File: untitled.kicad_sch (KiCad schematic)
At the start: 30 parts, among them IC1 ILD206T, IC10 ILD206T, IC2 ILD206T, IC3 ILD206T, IC4 ILD206T, IC5 ILD206T, IC6 ILD206T, IC7 ILD206T, IC8 ILD206T, IC9 ILD206T, J1 1147330000, J2 1147330000, J3 1147330000, K1 G2RL-1-H, K2 G2RL-1-H, K3 G2RL-1-H, U1 ULN2003A, U2 5-1415390-1, U3 5-1415390-1, U4 5-1415390-1

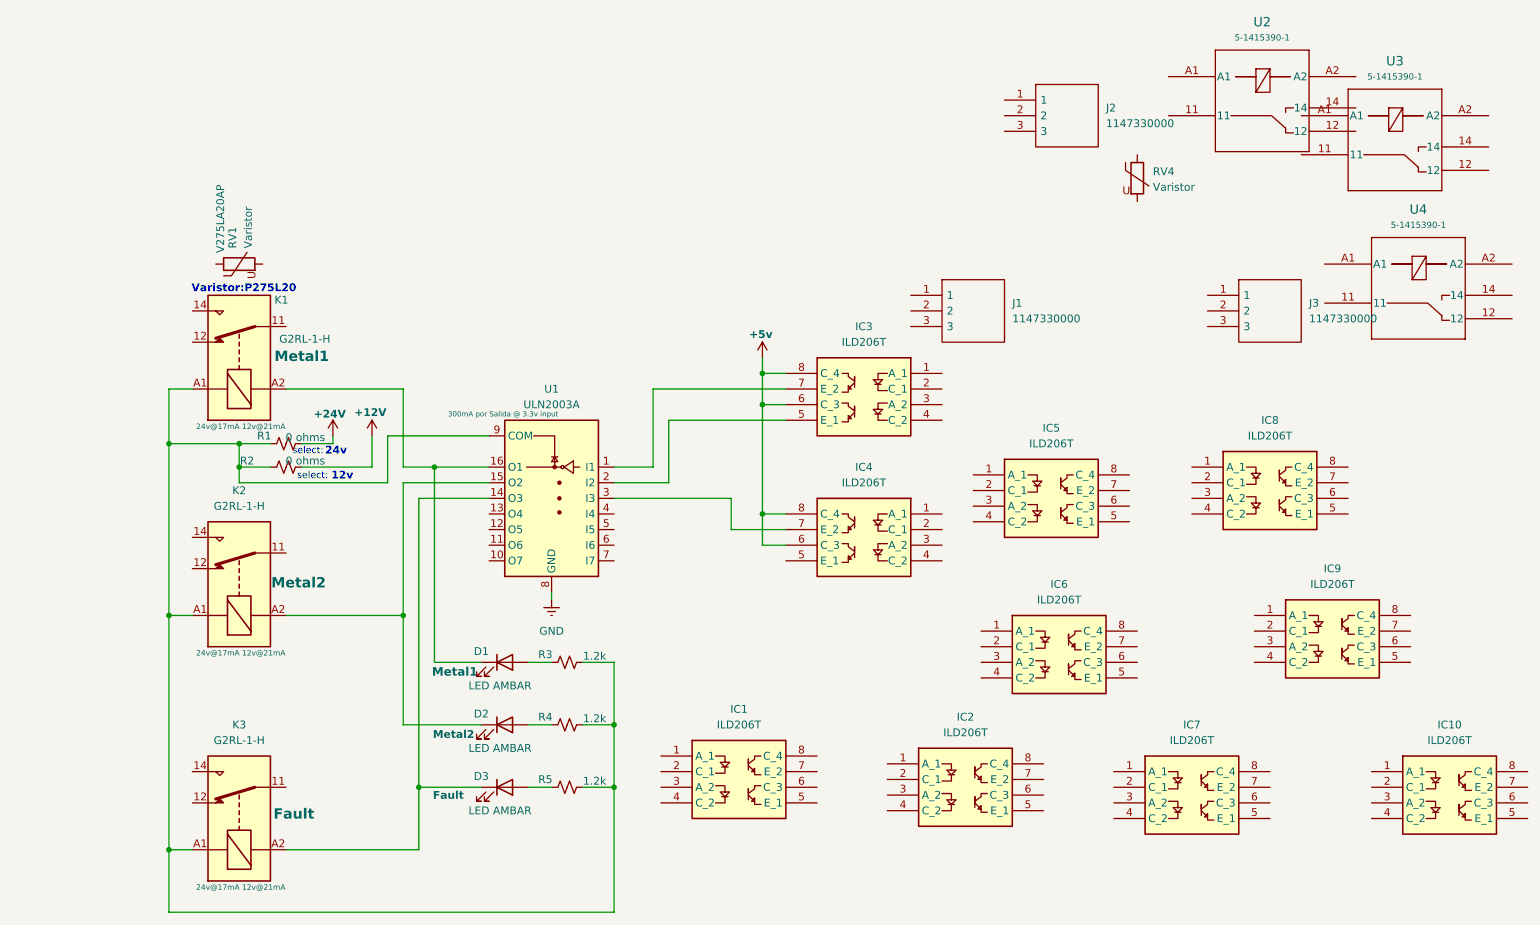
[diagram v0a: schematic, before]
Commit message: 13-Mayo26 se agrego hoja de procesador y USB
hoja de USB AL 95% HOJA DEL procesador al 75%
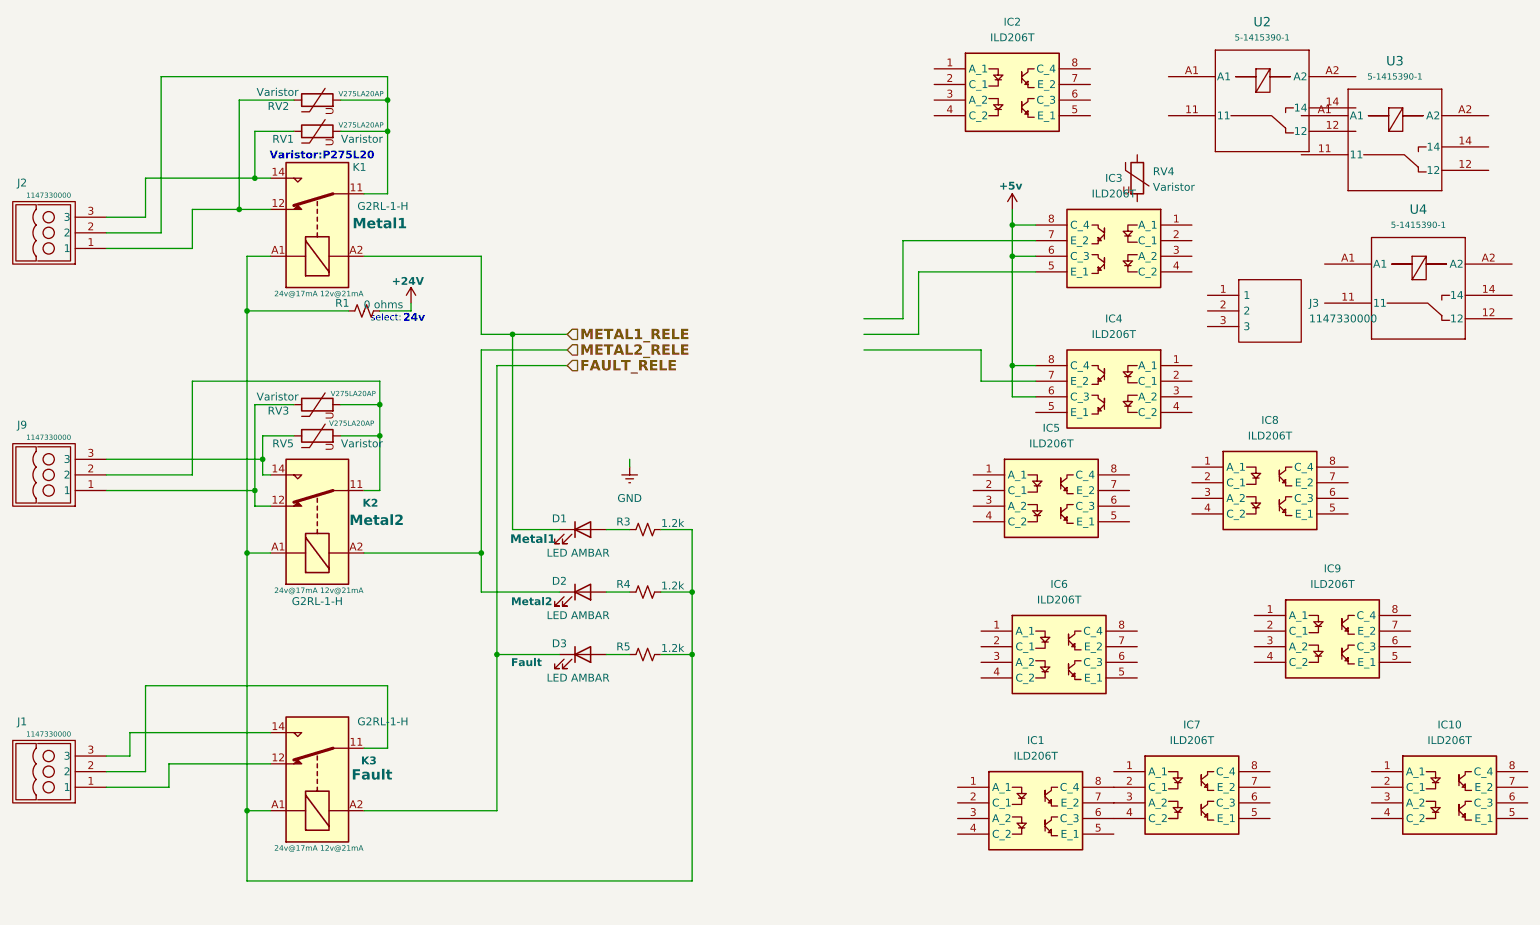
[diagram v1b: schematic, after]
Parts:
- removed R2: 0 ohms, symbol Device:R_Small_US
- removed U1: ULN2003A, symbol Transistor_Array:ULN2003A
- added J9: 1147330000, CONECTORES GRACIDA:3POS-5.08PITCH, symbol CONECTORES GRACIDA:1147330000
- added RV2, RV3, RV5: Varistor, Varistor:RV_Disc_D12mm_W3.9mm_P7.5mm, symbol Device:Varistor
- J1, J2: Mouser (none) -> 470-1147330000; Mouser Part Number 470-1147330000 -> (none); Mouser Price/Stock https://www.mouser.co.uk/ProductDetail/Weidmuller/114733000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 -> (none); Price (none) -> 2.41
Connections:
- net at J1.1: now also K3.12
- net at J1.2: now also K3.11
- net at J1.3: now also K3.14
- net METAL1_RELE: now reaches D1.1 (K), K1.A2
- net at IC1.6 (C_3): now also IC7.4 (C_2)
- net at IC1.7 (E_2): now also IC7.3 (A_2)
- net at IC1.8 (C_4): now also IC7.2 (C_1)
- net FAULT_RELE: now reaches D3.1 (K), K3.A2
- net at K1.11: now also J2.2, RV1.2, RV2.2
- net at K1.12: now also J2.1, RV2.1
- net at K1.14: now also J2.3, RV1.1
- net METAL2_RELE: now reaches D2.1 (K), K2.A2
- net at K2.11: now also J9.2, RV3.2, RV5.2
- net at K2.12: now also J9.1, RV3.1
- net at K2.14: now also J9.3, RV5.1
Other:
- note removed: "12v"
- moved on the sheet: D1, D2, D3, IC1, IC2, IC3, IC4, K1, K2, K3, R1, R3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

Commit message: 14-Mayo-26
se agregaron varias sheet de esquematico crecio al 80% la parte de esquematico
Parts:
- removed IC1, IC10, IC2, IC3, IC4, IC5, IC6, IC7, IC8, IC9: ILD206T, SOIC:SOIC 8, symbol OPTOACOPLADORES:ILD206T
- removed J3: 1147330000, CONECTORES GRACIDA:3POS-5.08PITCH, symbol CONECTORES GRACIDA:1147330000
- removed RV4: Varistor, Varistor:RV_Disc_D12mm_W3.9mm_P7.5mm, symbol Device:Varistor
- removed U2, U3, U4: 5-1415390-1, RELAYS GRACIDA:5-1415390-1, symbol RELAYS_GRACIDA:5-1415390-1
- renumbered J2 to J1, J9 to J2, J1 to J3, R3 to R2, R4 to R3, R5 to R4, RV2 to RV1, RV1 to RV2, RV5 to RV4

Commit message: 22 mayo 26 actualizacion
se actualizo la PCB para la rama laptop Antigua
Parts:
- J1, J2, J3: Mouser Part Number (none) -> 470-1147330000; Mouser Price/Stock (none) -> https://www.mouser.co.uk/ProductDetail/Weidmuller/114733000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
- renumbered R1 to R3, R2 to R4, R3 to R5, R4 to R6
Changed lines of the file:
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@@
 		(on_board yes)
 		(dnp no)
-		(property "Reference" "R2"
+		(property "Reference" "R4"
 			(at 133.604 96.52 90)
 			(effects
@@
 			)
 		)
-		(property "Description" "1.2k 5% 0603"
+		(property "Description" "Resistor, small US symbol"
 			(at 137.16 97.79 0)
 			(effects
@@
 			(project "01_IO-ASD-PLUS"
 				(path "/38a2da3c-ed29-422f-ab41-066ccf490e61/2e698a92-0ed9-457a-8ea3-5be56f6a1bd4"
-					(reference "R2")
+					(reference "R4")
 					(unit 1)
 				)
@@
 			)
 		)
-		(property "Description" "LED AMBAR"
+		(property "Description" "Light emitting diode"
 			(at 126.238 101.6 0)
 			(effects
@@
 		(on_board yes)
 		(dnp no)
-		(property "Reference" "#PWR01"
+		(property "Reference" "#PWR02"
 			(at 99.06 64.77 0)
 			(effects
@@
 			(project ""
 				(path "/38a2da3c-ed29-422f-ab41-066ccf490e61/2e698a92-0ed9-457a-8ea3-5be56f6a1bd4"
-					(reference "#PWR01")
+					(reference "#PWR02")
 					(unit 1)
 				)
@@
 		(on_board yes)
 		(dnp no)
-		(property "Reference" "R1"
+		(property "Reference" "R3"
 			(at 87.884 60.96 90)
 			(effects
@@
 			)
 		)
-		(property "Description" "Thick Film Resistors D11/CRCW0603 100 23R7 1% ET6 E3"
+		(property "Description" "Resistor, small US symbol"
 			(at 91.44 62.23 0)
 			(effects
@@
 			(project ""
 				(path "/38a2da3c-ed29-422f-ab41-066ccf490e61/2e698a92-0ed9-457a-8ea3-5be56f6a1bd4"
-					(reference "R1")
+					(reference "R3")
 					(unit 1)
 				)
@@
 			)
 		)
-		(property "Description" "LED AMBAR"
+		(property "Description" "Light emitting diode"
 			(at 126.238 121.92 0)
 			(effects
@@
 		(on_board yes)
 		(dnp no)
-		(property "Reference" "R4"
+		(property "Reference" "R6"
 			(at 133.604 116.84 90)
 			(effects
@@
 			)
 		)
-		(property "Description" "1.2k 5% 0603"
+		(property "Description" "Resistor, small US symbol"
 			(at 137.16 118.11 0)
 			(effects
@@
 			(project "01_IO-ASD-PLUS"
 				(path "/38a2da3c-ed29-422f-ab41-066ccf490e61/2e698a92-0ed9-457a-8ea3-5be56f6a1bd4"
-					(reference "R4")
+					(reference "R6")
 					(unit 1)
 				)
@@
 	)
 	(symbol
-		(lib_name "1147330000_1")
 		(lib_id "CONECTORES GRACIDA:1147330000")
 		(at 49.53 139.7 180)
@@
 		)
 		(property "Price" "2.41"
+			(at 33.02 119.38 0)
+			(effects
+				(font
+					(size 1.27 1.27)
+				)
+				(justify left)
+				(hide yes)
+			)
+		)
+		(property "Mouser Part Number" "470-1147330000"
+			(at 33.02 127 0)
+			(effects
+				(font
+					(size 1.27 1.27)
+				)
+				(justify left)
+				(hide yes)
+			)
+		)
+		(property "Mouser Price/Stock" "https://www.mouser.co.uk/ProductDetail/Weidmuller/1147330000?qs=WJDKaGZ8K%252B4exlyHM6mvUQ%3D%3D"
+			(at 33.02 124.46 0)
+			(effects
+				(font
+					(size 1.27 1.27)
+				)
+				(justify left)
+				(hide yes)
+			)
+		)
+		(property "Arrow Price/Stock" ""
 			(at 33.02 119.38 0)
 			(effects
@@
 		(dnp no)
 		(fields_autoplaced yes)
-		(property "Reference" "#PWR02"
+		(property "Reference" "#PWR03"
 			(at 134.62 93.98 0)
 			(effects
@@
 			(project ""
 				(path "/38a2da3c-ed29-422f-ab41-066ccf490e61/2e698a92-0ed9-457a-8ea3-5be56f6a1bd4"
-					(reference "#PWR02")
+					(reference "#PWR03")
 					(unit 1)
 				)
@@
 			)
 		)
-		(property "Description" "LED AMBAR"
+		(property "Description" "Light emitting diode"
 			(at 126.238 111.76 0)
 			(effects
@@
 	)
 	(symbol
-		(lib_name "1147330000_1")
 		(lib_id "CONECTORES GRACIDA:1147330000")
 		(at 49.53 91.44 180)
@@
 		)
 		(property "Price" "2.41"
+			(at 33.02 71.12 0)
+			(effects
+				(font
+					(size 1.27 1.27)
+				)
+				(justify left)
+				(hide yes)
+			)
+		)
+		(property "Mouser Part Number" "470-1147330000"
+			(at 33.02 78.74 0)
+			(effects
+				(font
+					(size 1.27 1.27)
+				)
+				(justify left)
+				(hide yes)
+			)
+		)
+		(property "Mouser Price/Stock" "https://www.mouser.co.uk/ProductDetail/Weidmuller/1147330000?qs=WJDKaGZ8K%252B4exlyHM6mvUQ%3D%3D"
+			(at 33.02 76.2 0)
+			(effects
+				(font
+					(size 1.27 1.27)
+				)
+				(justify left)
+				(hide yes)
+			)
+		)
+		(property "Arrow Price/Stock" ""
 			(at 33.02 71.12 0)
 			(effects
@@
 			)
 		)
-		(property "Description" "P275L20 = Varistor (resistencia variable dependiente del voltaje)  Su función: proteger circuitos contra sobretensiones (rayos, picos de voltaje)Voltaje AC máx: 275V (ideal para 220V)  Corriente pico: ~4.5-6.5kA  Diámetro: 14-20mm, Varistores 275V 450pF  , Parámetro Valor Diámetro del disco (cuerpo) 14 mm (0.55 in)  Ancho (con las patillas) 5.6 mm (0.22 in)  Altura total 20 mm (0.79 in)  Longitud de la patilla (terminal) 25.4 mm (1.0 in)  Paso de las patillas (distancia entre ellas) 8.5 mm (0.33 in) (según algunas fuentes, 7.5 mm)"
+		(property "Description" "Voltage dependent resistor"
 			(at 83.82 77.47 0)
 			(effects
@@
 		(on_board yes)
 		(dnp no)
-		(property "Reference" "R3"
+		(property "Reference" "R5"
 			(at 133.604 106.68 90)
 			(effects
@@
 			)
 		)
-		(property "Description" "1.2k 5% 0603"
+		(property "Description" "Resistor, small US symbol"
 			(at 137.16 107.95 0)
 			(effects
@@
 			(project "01_IO-ASD-PLUS"
 				(path "/38a2da3c-ed29-422f-ab41-066ccf490e61/2e698a92-0ed9-457a-8ea3-5be56f6a1bd4"
-					(reference "R3")
+					(reference "R5")
 					(unit 1)
 				)
@@
 			)
 		)
-		(property "Description" "P275L20 = Varistor (resistencia variable dependiente del voltaje)  Su función: proteger circuitos contra sobretensiones (rayos, picos de voltaje)Voltaje AC máx: 275V (ideal para 220V)  Corriente pico: ~4.5-6.5kA  Diámetro: 14-20mm, Varistores 275V 450pF  , Parámetro Valor Diámetro del disco (cuerpo) 14 mm (0.55 in)  Ancho (con las patillas) 5.6 mm (0.22 in)  Altura total 20 mm (0.79 in)  Longitud de la patilla (terminal) 25.4 mm (1.0 in)  Paso de las patillas (distancia entre ellas) 8.5 mm (0.33 in) (según algunas fuentes, 7.5 mm)"
+		(property "Description" "Voltage dependent resistor"
 			(at 83.82 27.94 0)
 			(effects
@@
 			)
 		)
-		(property "Description" "P275L20 = Varistor (resistencia variable dependiente del voltaje)  Su función: proteger circuitos contra sobretensiones (rayos, picos de voltaje)Voltaje AC máx: 275V (ideal para 220V)  Corriente pico: ~4.5-6.5kA  Diámetro: 14-20mm, Varistores 275V 450pF  , Parámetro Valor Diámetro del disco (cuerpo) 14 mm (0.55 in)  Ancho (con las patillas) 5.6 mm (0.22 in)  Altura total 20 mm (0.79 in)  Longitud de la patilla (terminal) 25.4 mm (1.0 in)  Paso de las patillas (distancia entre ellas) 8.5 mm (0.33 in) (según algunas fuentes, 7.5 mm)"
+		(property "Description" "Voltage dependent resistor"
 			(at 83.82 33.02 0)
 			(effects
@@
 			)
 		)
-		(property "Description" "P275L20 = Varistor (resistencia variable dependiente del voltaje)  Su función: proteger circuitos contra sobretensiones (rayos, picos de voltaje)Voltaje AC máx: 275V (ideal para 220V)  Corriente pico: ~4.5-6.5kA  Diámetro: 14-20mm, Varistores 275V 450pF  , Parámetro Valor Diámetro del disco (cuerpo) 14 mm (0.55 in)  Ancho (con las patillas) 5.6 mm (0.22 in)  Altura total 20 mm (0.79 in)  Longitud de la patilla (terminal) 25.4 mm (1.0 in)  Paso de las patillas (distancia entre ellas) 8.5 mm (0.33 in) (según algunas fuentes, 7.5 mm)"
+		(property "Description" "Voltage dependent resistor"
 			(at 83.82 82.55 0)
 			(effects
@@
 	)
 	(symbol
-		(lib_name "1147330000_1")
 		(lib_id "CONECTORES GRACIDA:1147330000")
 		(at 49.53 52.07 180)
@@
 			(at 33.02 31.75 0)
 			(effects
+				(font
+					(size 1.27 1.27)
+				)
+				(justify left)
+				(hide yes)
+			)
+		)
+		(property "Mouser Part Number" "470-1147330000"
+			(at 33.02 39.37 0)
+			(effects
+				(font
+					(size 1.27 1.27)
+				)
+				(justify left)
+				(hide yes)
+			)
+		)
+		(property "Mouser Price/Stock" "https://www.mouser.co.uk/ProductDetail/Weidmuller/1147330000?qs=WJDKaGZ8K%252B4exlyHM6mvUQ%3D%3D"
+			(at 33.02 36.83 0)
+			(effects
+				(font
+					(size 1.27 1.27)
+				)
+				(justify left)
+				(hide yes)
+			)
+		)
+		(property "Arrow Price/Stock" ""
+			(at 33.02 31.75 0)
+			(effects

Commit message: 05/06/26
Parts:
- R3: footprint (none) -> Resistor_SMD:R_0603_1608Metric_Pad0.98x0.95mm_HandSolder
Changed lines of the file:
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@@
 			)
 		)
-		(property "Footprint" ""
+		(property "Footprint" "Resistor_SMD:R_0603_1608Metric_Pad0.98x0.95mm_HandSolder"
 			(at 91.44 62.23 0)
 			(effects
